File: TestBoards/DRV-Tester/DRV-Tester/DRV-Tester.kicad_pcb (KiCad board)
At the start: 2 copper layers, 24 parts, among them J1 Screw_Terminal_01x02, J10 Conn_02x04_Odd_Even, J11 Conn_02x04_Odd_Even, J2 Screw_Terminal_01x02, J3 Screw_Terminal_01x02, J4 Screw_Terminal_01x02, J5 Screw_Terminal_01x02, J6 Screw_Terminal_01x02, J7 Conn_02x04_Odd_Even, J8 Conn_02x04_Odd_Even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

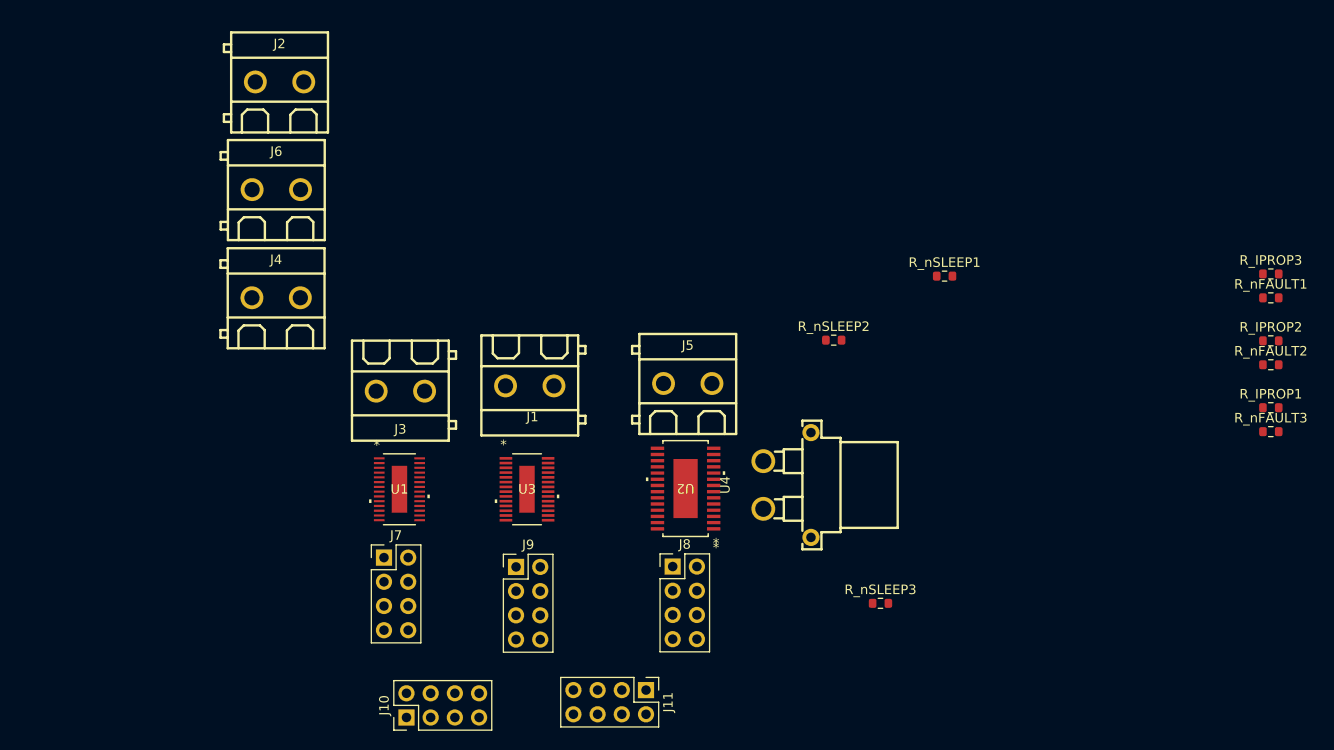
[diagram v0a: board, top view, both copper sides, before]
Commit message: update tester board with layout
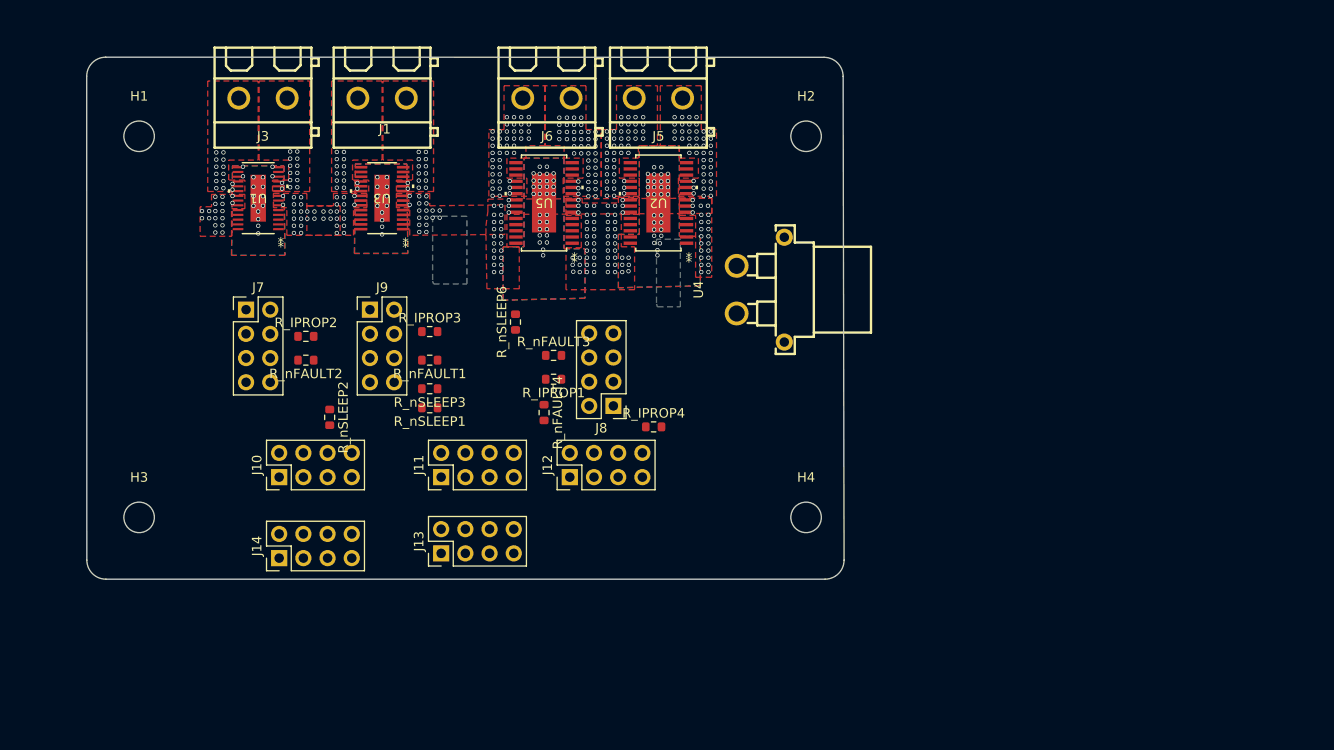
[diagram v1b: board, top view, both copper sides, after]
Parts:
- removed J2, J4: Screw_Terminal_01x02, easyeda2kicad:CONN-TH_P5.08_KF128-5.08-2P
- added H1: MountingHole_Pad, MountingHole:MountingHole_3.2mm_M3, F.Cu at (78.0, 72.5)
- added H2: MountingHole_Pad, MountingHole:MountingHole_3.2mm_M3, F.Cu at (148.0, 72.5)
- added H3: MountingHole_Pad, MountingHole:MountingHole_3.2mm_M3, F.Cu at (78.0, 112.5)
- added H4: MountingHole_Pad, MountingHole:MountingHole_3.2mm_M3, F.Cu at (148.0, 112.5)
- added J12: Conn_02x04_Odd_Even, Connector_PinHeader_2.54mm:PinHeader_2x04_P2.54mm_Vertical, F.Cu at (123.2, 108.3)
- added J13: Conn_02x04_Odd_Even, Connector_PinHeader_2.54mm:PinHeader_2x04_P2.54mm_Vertical, F.Cu at (109.7, 116.3)
- added J14: Conn_02x04_Odd_Even, Connector_PinHeader_2.54mm:PinHeader_2x04_P2.54mm_Vertical, F.Cu at (92.7, 116.8)
- added R_IPROP4: 820, Resistor_SMD:R_0603_1608Metric, F.Cu at (132.0, 103.0)
- added R_nFAULT4: 820, Resistor_SMD:R_0603_1608Metric, F.Cu at (120.5, 101.5)
- added R_nSLEEP6: 8.2k, Resistor_SMD:R_0603_1608Metric, F.Cu at (117.5, 92.0)
- added U5: PDRV8245SPWPQ1, PDRV8245SPWPQ1:U_PWP0028R_TEX, F.Cu at (120.5, 79.5)
- moved R_nFAULT2 101.3 mm to (95.5, 96.0), turned to 180 degrees
- moved R_IPROP2 101.3 mm to (95.5, 93.5)
- moved R_nFAULT1 88.5 mm to (108.5, 96.0), turned to 180 degrees
- moved R_IPROP3 88.5 mm to (108.5, 93.0)
- moved R_nFAULT3 75.7 mm to (121.5, 95.5)
- moved R_IPROP1 75.3 mm to (121.5, 98.0), turned to 180 degrees
- moved R_nSLEEP1 55.8 mm to (108.5, 101.0), turned to 180 degrees
- moved R_nSLEEP2 53.5 mm to (98.0, 102.0), turned to -90 degrees
- moved R_nSLEEP3 52.4 mm to (108.5, 99.0), turned to 180 degrees
- moved U3 34.1 mm to (103.5, 79.0), turned to 180 degrees
- moved J3 34.0 mm to (91.0, 68.5)
- moved U1 34.0 mm to (90.5, 79.0), turned to 180 degrees
- moved J1 33.9 mm to (103.5, 68.5)
- moved J9 31.1 mm to (102.2, 90.7)
- moved J11 31.0 mm to (109.7, 108.3), turned to 90 degrees
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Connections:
- J1 pad 1: /DRV8243/OUT2 -> /DRV8243/OUT1
- J1 pad 2: /DRV8243/OUT1 -> /DRV8243/OUT2
- J10 pad 8: /COM_GPIO/3v3_VCC -> 3V3
- J11 pad 2: unconnected-(J11-Pin_2-Pad2) -> DRV4_CS
- J11 pad 4: unconnected-(J11-Pin_4-Pad4) -> DRV5_CS
- J11 pad 6: unconnected-(J11-Pin_6-Pad6) -> DRV6_CS
- J3 pad 1: /DRV8244/OUT2 -> /DRV8244/OUT1
- J3 pad 2: /DRV8244/OUT1 -> /DRV8244/OUT2
- J5 pad 1: /DRV8245/OUT2 -> /DRV8245/OUT1
- J5 pad 2: /DRV8245/OUT1 -> /DRV8245/OUT2
- J6 pad 1: /DRV8245/OUT4 -> /DRV8245/OUT3
- J6 pad 2: /DRV8245/OUT3 -> /DRV8245/OUT4
- J7 pad 8: /DRV1_GPIO1/3v3_VCC -> 3V3
- J8 pad 8: /DRV1_GPIO/3v3_VCC -> 3V3
- J9 pad 8: /DRV1_GPIO2/3v3_VCC -> 3V3
- R_nFAULT1 pad 1: /DRV1_GPIO2/3v3_VCC -> 3V3
- R_nFAULT2 pad 1: /DRV1_GPIO1/3v3_VCC -> 3V3
- R_nFAULT3 pad 1: /DRV1_GPIO/3v3_VCC -> 3V3
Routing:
- net VM: vias 0 -> 176
- net GND: vias 0 -> 88
- net /DRV8245/OUT4: vias 0 -> 43
- net /DRV8245/OUT3: vias 0 -> 43
- net /DRV8245/OUT2: vias 0 -> 43
- net /DRV8245/OUT1: vias 0 -> 55
- net /DRV8244/OUT2: vias 0 -> 26
- net /DRV8244/OUT1: vias 0 -> 14
- net /DRV8243/OUT2: vias 0 -> 2
- net /DRV8243/OUT1: vias 0 -> 2
- added copper zone on B.Cu, net (none)
- added copper zone on F.Cu, net (none)
- added copper zone on F.Cu, net /DRV8243/OUT1
- added copper zone on In1.Cu, net /DRV8243/OUT1
- added copper zone on F.Cu, net /DRV8243/OUT2
- added copper zone on In1.Cu, net /DRV8243/OUT2
- added copper zone on F.Cu, net /DRV8244/OUT1
- added copper zone on In1.Cu, net /DRV8244/OUT1
- added copper zone on F.Cu, net /DRV8244/OUT2
- added copper zone on In1.Cu, net /DRV8244/OUT2
- added copper zone on F.Cu, net /DRV8245/OUT1
- added copper zone on F.Cu, net /DRV8245/OUT2
- added copper zone on F.Cu, net /DRV8245/OUT3
- added copper zone on F.Cu, net /DRV8245/OUT4
- added copper zone on B.Cu, net GND
- added copper zone on F.Cu, net GND
- added copper zone on In2.Cu, net GND
- added copper zone on F.Cu, net VM
- added copper zone on In1.Cu, net VM
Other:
- board outline added: 79.5 x 54.8 mm
- copper layers 2 -> 4

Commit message: finish layout for stupid lil test board
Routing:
- net GND: track 0.00 -> 193.5 mm, vias 88 -> 90
- net NSLEEP: track 0.00 -> 164.9 mm, vias 0 -> 2
- net M_MOSI: track 0.00 -> 131.4 mm, vias 0 -> 3
- net 3V3: track 0.00 -> 130.2 mm, vias 0 -> 5
- net M_MISO: track 0.00 -> 118.6 mm, vias 0 -> 3
- net M_SCLK: track 0.00 -> 110.3 mm, vias 0 -> 4
- net DRV_OFF: track 0.00 -> 100.7 mm, vias 0 -> 3
- net DRV2_CS: track 0.00 -> 59.0 mm, vias 0 -> 1
- net DRV6_CS: track 0.00 -> 54.3 mm
- net IPROPI_2: track 0.00 -> 53.2 mm, vias 0 -> 1
- net DRV3_CS: track 0.00 -> 45.5 mm, vias 0 -> 1
- net IPROPI_6: track 0.00 -> 40.3 mm, vias 0 -> 1
- net /DRV1_GPIO/N_FAULT2: track 0.00 -> 31.1 mm, vias 0 -> 1
- net /DRV1_GPIO/IN2: track 0.00 -> 29.6 mm, vias 0 -> 1
- net DRV1_CS: track 0.00 -> 29.5 mm, vias 0 -> 1
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- added copper zone on In2.Cu, net /DRV8243/OUT1
- added copper zone on In2.Cu, net /DRV8243/OUT2
- added copper zone on In2.Cu, net /DRV8244/OUT1
- added copper zone on In2.Cu, net /DRV8244/OUT2
- added copper zone on In1.Cu, net /DRV8245/OUT1
- added copper zone on In2.Cu, net /DRV8245/OUT1
- added copper zone on In1.Cu, net /DRV8245/OUT2
- added copper zone on In2.Cu, net /DRV8245/OUT2
- added copper zone on In1.Cu, net /DRV8245/OUT3
- added copper zone on In2.Cu, net /DRV8245/OUT3
- added copper zone on In1.Cu, net /DRV8245/OUT4
- added copper zone on In2.Cu, net /DRV8245/OUT4
- added copper zone on In1.Cu, net GND

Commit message: add caps and LEDs to testboard
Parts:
- added C1: 22uF, Capacitor_SMD:C_1210_3225Metric, F.Cu at (140.9, 78.8)
- added C2: 10uF, Capacitor_SMD:C_1210_3225Metric, F.Cu at (145.2, 78.8)
- added C3: 10uF, Capacitor_SMD:C_0603_1608Metric, F.Cu at (81.9, 82.9)
- added C4: 10uF, Capacitor_SMD:C_1210_3225Metric, F.Cu at (149.4, 78.8)
- added C5: 10uF, Capacitor_SMD:C_1210_3225Metric, F.Cu at (81.4, 80.4)
- added C6: EEU-FC1J101LB, SamacSys_Parts:CAPPRD350W65D800H1650, F.Cu at (83.6, 103.6)
- added C7: EEU-FC1J101LB, SamacSys_Parts:CAPPRD350W65D800H1650, F.Cu at (83.8, 95.2)
- added C8: EEU-FC1J101LB, SamacSys_Parts:CAPPRD350W65D800H1650, F.Cu at (145.5, 98.8)
- added C9: EEU-FC1J101LB, SamacSys_Parts:CAPPRD350W65D800H1650, F.Cu at (83.7, 86.8)
- added R1: 500, Resistor_SMD:R_0603_1608Metric, F.Cu at (139.4, 108.2)
- added R2: 8.2k, Resistor_SMD:R_0603_1608Metric, F.Cu at (142.2, 108.2)
- added V3v1: LED, LED_SMD:LED_0603_1608Metric, F.Cu at (136.6, 108.2)
- added VM1: LED, LED_SMD:LED_0603_1608Metric, F.Cu at (145.0, 108.2)
- moved R_nSLEEP2 43.3 mm to (139.5, 114.5), turned to 90 degrees
- moved R_nSLEEP1 36.6 mm to (142.5, 114.5), turned to 90 degrees
- moved R_IPROP2 35.0 mm to (123.5, 114.5), turned to -90 degrees
- moved R_nSLEEP3 32.0 mm to (136.5, 114.5), turned to 90 degrees
- moved R_nFAULT2 31.6 mm to (124.5, 108.5), turned to 90 degrees
- moved R_IPROP3 28.0 mm to (126.5, 114.5), turned to -90 degrees
- moved R_nSLEEP6 27.6 mm to (133.5, 114.5)
- moved R_nFAULT1 25.3 mm to (130.5, 108.5), turned to 90 degrees
- moved R_nFAULT3 17.8 mm to (133.7, 108.4), turned to 90 degrees
- moved J12 17.5 mm to (120.5, 91.0), turned to 0 degrees
- moved R_IPROP1 16.5 mm to (120.5, 114.5), turned to -90 degrees
- moved R_IPROP4 11.8 mm to (129.5, 114.5), turned to -90 degrees
- moved J8 10.5 mm to (131.5, 91.0), turned to 0 degrees
- moved R_nFAULT4 9.90 mm to (127.5, 108.5), turned to 90 degrees
- moved J7 0.30 mm to (89.2, 91.0)
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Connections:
- J10 pad 1: M_SCLK -> M_MISO
- J10 pad 2: GND -> M_SCLK
- J10 pad 3: unconnected-(J10-Pin_3-Pad3) -> M_MOSI
- J10 pad 4: DRV_OFF -> 3V3
- J10 pad 5: M_MOSI -> GND
- J10 pad 6: NSLEEP -> GND
- J10 pad 7: M_MISO -> NSLEEP
- J10 pad 8: 3V3 -> DRV_OFF
- J12 pad 1: unconnected-(J12-Pin_1-Pad1) -> IPROPI_6
- J12 pad 2: GND -> /DRV1_GPIO/IN4
- J12 pad 3: unconnected-(J12-Pin_3-Pad3) -> /DRV1_GPIO/N_FAULT2
- J12 pad 4: IPROPI_6 -> /DRV1_GPIO/IN3
- J12 pad 5: unconnected-(J12-Pin_5-Pad5) -> 3V3
- J12 pad 6: /DRV1_GPIO/N_FAULT2 -> 3V3
- J12 pad 7: unconnected-(J12-Pin_7-Pad7) -> GND
- J12 pad 8: 3V3 -> GND
- J13 pad 1: unconnected-(J13-Pin_1-Pad1) -> /DRV1_GPIO1/IPROPI2
- J13 pad 2: GND -> /DRV1_GPIO1/IN4
- J13 pad 3: unconnected-(J13-Pin_3-Pad3) -> /DRV1_GPIO1/N_FAULT2
- J13 pad 4: /DRV1_GPIO1/IPROPI2 -> /DRV1_GPIO1/IN3
- J13 pad 5: unconnected-(J13-Pin_5-Pad5) -> 3V3
- J13 pad 6: /DRV1_GPIO1/N_FAULT2 -> 3V3
- J13 pad 7: unconnected-(J13-Pin_7-Pad7) -> GND
- J13 pad 8: 3V3 -> GND
- J14 pad 1: unconnected-(J14-Pin_1-Pad1) -> /DRV1_GPIO2/IPROPI2
- J14 pad 2: GND -> /DRV1_GPIO2/IN4
- J14 pad 3: unconnected-(J14-Pin_3-Pad3) -> /DRV1_GPIO2/N_FAULT2
- J14 pad 4: /DRV1_GPIO2/IPROPI2 -> /DRV1_GPIO2/IN3
- J14 pad 5: unconnected-(J14-Pin_5-Pad5) -> 3V3
- J14 pad 6: /DRV1_GPIO2/N_FAULT2 -> 3V3
- J14 pad 7: unconnected-(J14-Pin_7-Pad7) -> GND
- J14 pad 8: 3V3 -> GND
- J7 pad 1: /DRV1_GPIO1/IN1 -> IPROPI_2
- J7 pad 2: GND -> /DRV1_GPIO1/IN1
- J7 pad 3: /DRV1_GPIO1/IN2 -> /DRV1_GPIO1/N_FAULT
- J7 pad 4: IPROPI_2 -> /DRV1_GPIO1/IN2
- J7 pad 5: /DRV1_GPIO1/IN3 -> 3V3
- J7 pad 6: /DRV1_GPIO1/N_FAULT -> 3V3
- J7 pad 7: /DRV1_GPIO1/IN4 -> GND
- J7 pad 8: 3V3 -> GND
- J8 pad 1: /DRV1_GPIO/IN1 -> IPROPI_3
- J8 pad 2: GND -> /DRV1_GPIO/IN1
- J8 pad 3: /DRV1_GPIO/IN2 -> /DRV1_GPIO/N_FAULT
- J8 pad 4: IPROPI_3 -> /DRV1_GPIO/IN2
- J8 pad 5: /DRV1_GPIO/IN3 -> 3V3
- J8 pad 6: /DRV1_GPIO/N_FAULT -> 3V3
- J8 pad 7: /DRV1_GPIO/IN4 -> GND
- J8 pad 8: 3V3 -> GND
- J9 pad 1: /DRV1_GPIO2/IN1 -> IPROPI_1
- J9 pad 2: GND -> /DRV1_GPIO2/IN1
- J9 pad 3: /DRV1_GPIO2/IN2 -> /DRV1_GPIO2/N_FAULT
- J9 pad 4: IPROPI_1 -> /DRV1_GPIO2/IN2
- J9 pad 5: /DRV1_GPIO2/IN3 -> 3V3
- J9 pad 6: /DRV1_GPIO2/N_FAULT -> 3V3
- J9 pad 7: /DRV1_GPIO2/IN4 -> GND
- J9 pad 8: 3V3 -> GND
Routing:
- net GND: track 193.5 -> 276.5 mm, vias 90 -> 92
- net VM: track 18.3 -> 88.2 mm, vias 167 -> 163
- net /DRV1_GPIO1/N_FAULT: track 20.0 -> 78.2 mm
- net IPROPI_1: track 3.01 -> 48.2 mm, vias 0 -> 2
- net IPROPI_2: track 53.2 -> 87.7 mm, vias 1 -> 3
- net /DRV1_GPIO2/N_FAULT: track 20.3 -> 52.5 mm
- net M_MOSI: track 131.4 -> 99.9 mm, vias 3 -> 4
- net M_MISO: track 118.6 -> 88.3 mm, vias 3 -> 4
- net DRV6_CS: track 54.3 -> 30.4 mm
- net M_SCLK: track 110.3 -> 87.1 mm
- net NSLEEP: track 164.9 -> 186.9 mm, vias 2 -> 0
- net IPROPI_3: track 25.3 -> 45.4 mm
- net /DRV1_GPIO/IN2: track 29.6 -> 13.3 mm, vias 1 -> 0
- net DRV2_CS: track 59.0 -> 43.0 mm
- net /DRV1_GPIO2/IN1: track 27.7 -> 13.1 mm
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
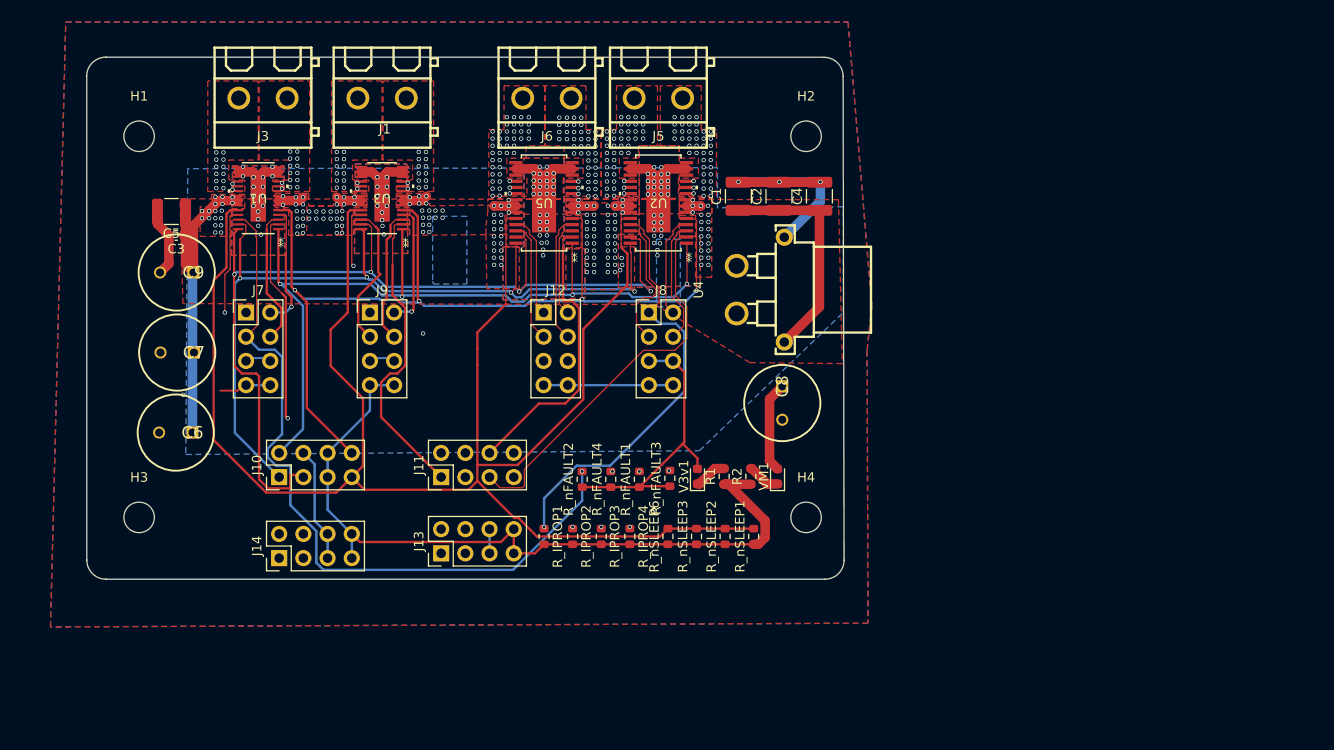
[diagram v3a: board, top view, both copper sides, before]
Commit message: Create initial driver for DRV824x drivers for ESP32 / SimpleFOC
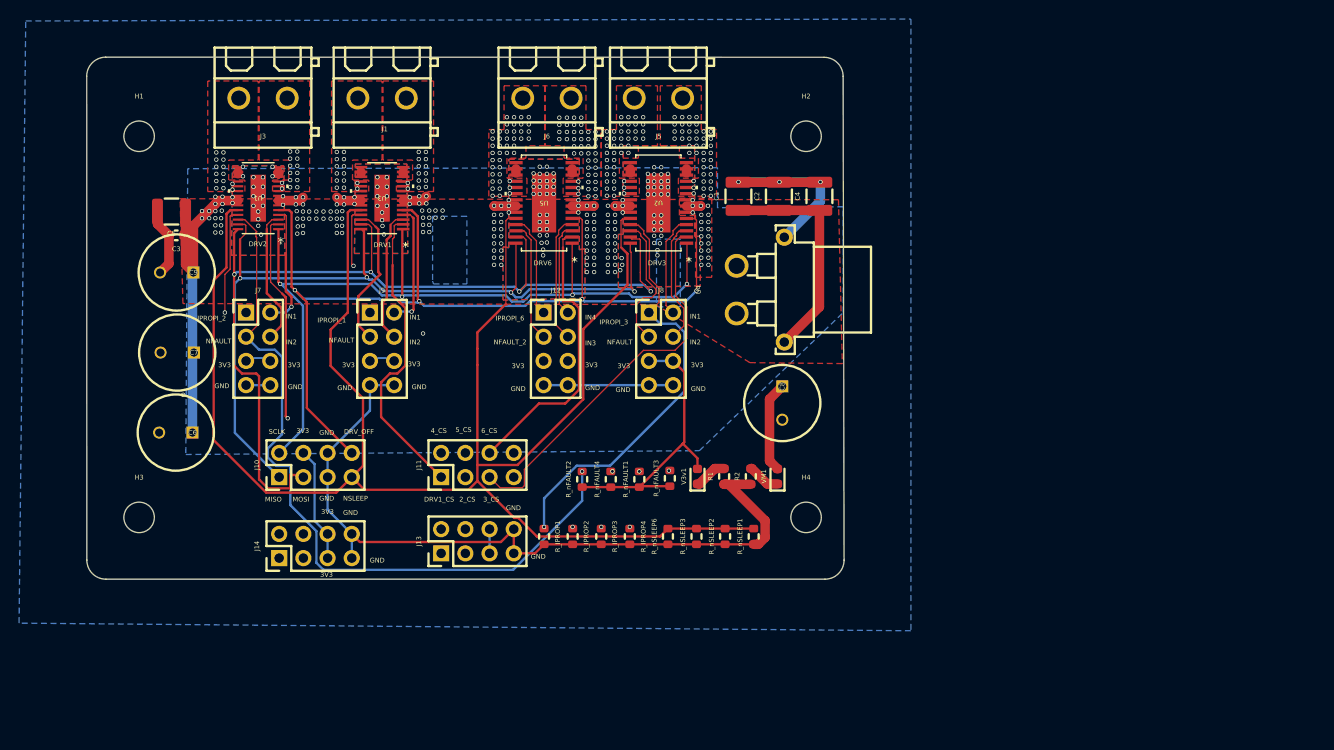
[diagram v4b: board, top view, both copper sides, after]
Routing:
- net GND: track 276.5 -> 255.5 mm
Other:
- board text added: "2_CS"
- board text added: "3V3"
- board text added: "3_CS"
- board text added: "4_CS"
- board text added: "5_CS"
- board text added: "6_CS"
- board text added: "DRV1"
- board text added: "DRV1_CS"
- board text added: "DRV2"
- board text added: "DRV3"
- board text added: "DRV6"
- board text added: "DRV_OFF"
- board text added: "GND"
- board text added: "IN1"
- board text added: "IN2"
- board text added: "IN3"
- board text added: "IN4"
- board text added: "IPROPI_1"
- board text added: "IPROPI_2"
- board text added: "IPROPI_3"
- board text added: "IPROPI_6"
- board text added: "MISO"
- board text added: "MOSI"
- board text added: "NFAULT"
- board text added: "NFAULT_2"
- board text added: "NSLEEP"
- board text added: "SCLK"
- board text added: "TestDrv Board for DRV824x parts 6/2024 Input V: 10 - 30V 3V3 / 5V logic capable"
